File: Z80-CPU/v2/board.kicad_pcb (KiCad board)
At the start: 2 copper layers, 254 x 134.6 mm, 162 parts, among them K1 CONN_3, K2 CONN_3, K4 CONN_3, P1 S100_MALE, P2 CONN_4X2, P3 CLK_CPU, P34 CONN_1, P35 CONN_1, P36 CONN_3X2, P37 CONN_2X2, P4 CONN_2X2, P5 CLK_CPU, P6 CLK_SEL, Q1 2N3904, Q2 ^^NPN-SOT23, Q3 ^^NPN-SOT23, Q4 ^^NPN-SOT23, Q5 ^^NPN-SOT23, Q6 ^^NPN-SOT23, Q7 ^^NPN-SOT23, SW2 DIPS_08, SW3 DIPS_08, SW4 DIPS_08, U1 Z80, U10 74LS165, U11 74LS165, U12 74LS373, U13 2732, U14 74LS682N, U16 74LS273, U17 74LS273, U19 74LS244, U2 74LS373, U20 74LS244, U21 74LS244, U22 74LS373, U23 74LS02, U24 74LS04, U25 74LS04, U26 74LS05, U27 74LS139, U28 74LS00, U29 74LS74, U3 74LS373, U30 74LS74, U31 74LS00, U32 74LS74, U33 74LS74, U34 74LS74, U35 74LS32, U36 74LS04, U37 74LS05, U38 74F04, U39 74S08, U4 74LS153, U40 74S00, U41 74LS27, U42 2.0000 MHz, U43 74LS11, U44 74LS32, U45 74LS02, U47 74LS04, U48 LDO_REG_7805, U49 74LS00, U5 74LS157, U6 74LS153, U7 74LS32, U8 74LS157, U9 74LS165

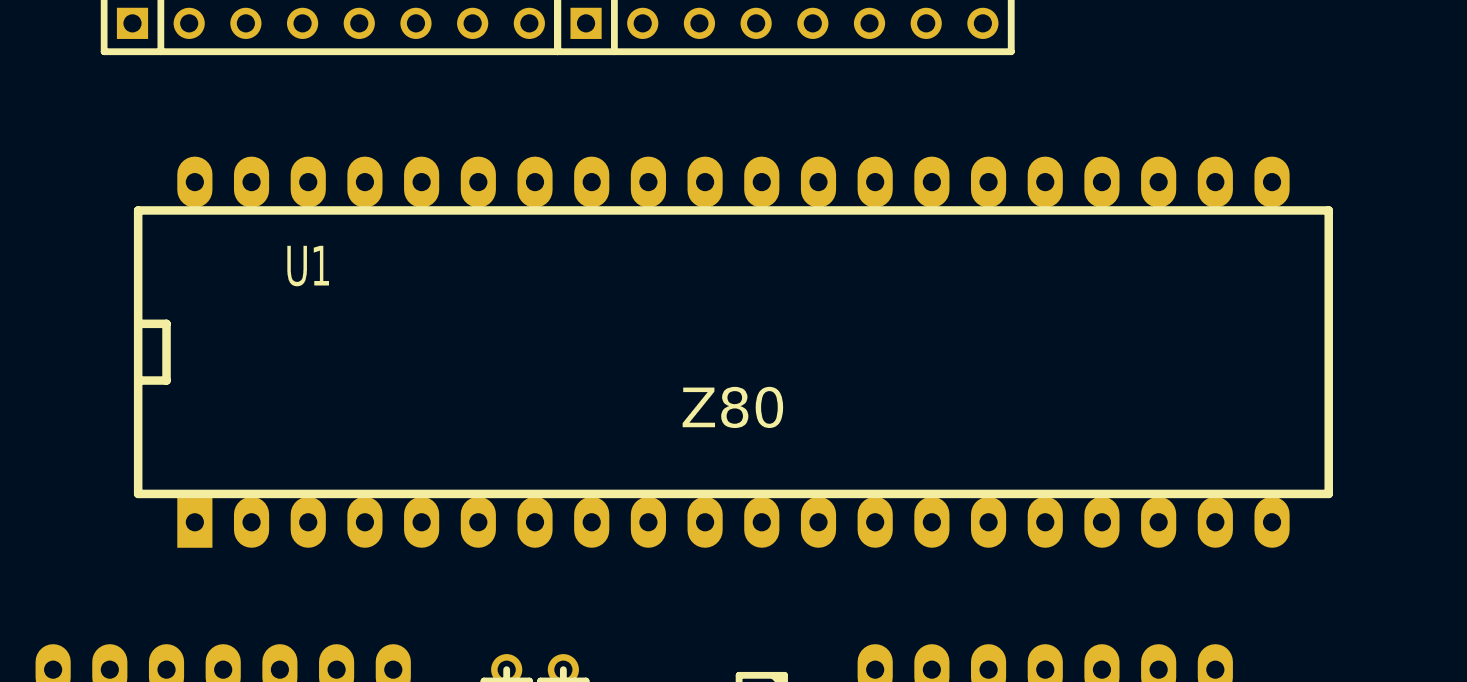
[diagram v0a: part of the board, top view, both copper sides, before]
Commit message: Z80-CPU v2: board layout (unrouted)
Source: S100 Z80 version2/backups/06-06-2014 2143
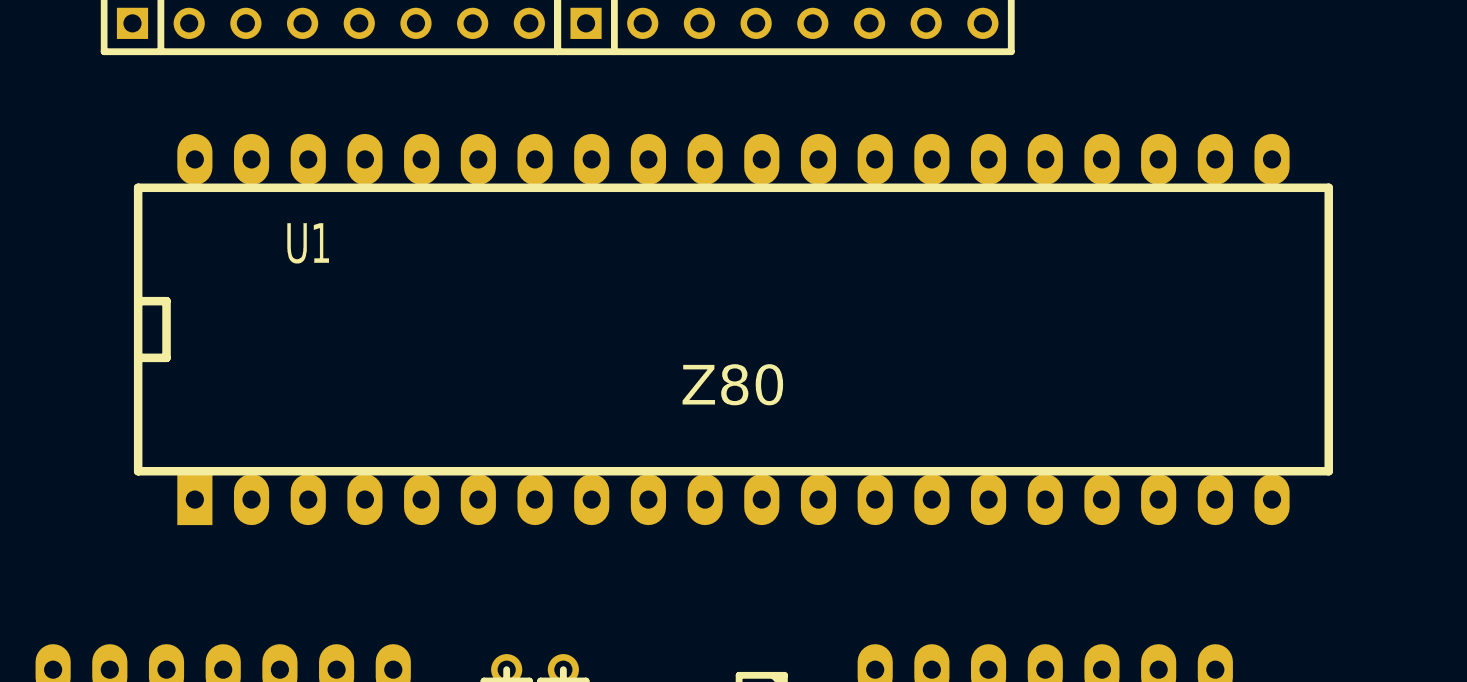
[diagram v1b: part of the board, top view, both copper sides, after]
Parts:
- moved U1 1.02 mm to (194.3, 55.9)
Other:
- net class Default: via_dia 0.5 -> 0.6
- net class gnd added: clearance 0.2032, trace_width 0.4, via_dia 0.6, via_drill 0.35
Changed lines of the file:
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@@
     (segment_width 0.381)
     (edge_width 0.381)
-    (via_size 0.5)
+    (via_size 0.6)
     (via_drill 0.35)
     (via_min_size 0.4)
@@
     (clearance 0.2032)
     (trace_width 0.2032)
-    (via_dia 0.5)
+    (via_dia 0.6)
     (via_drill 0.35)
     (uvia_dia 0.508)
@@
     (uvia_dia 0.508)
     (uvia_drill 0.2032)
-    (add_net GND)
     (add_net VCC)
   )
+  (net_class gnd ""
+    (clearance 0.2032)
+    (trace_width 0.4)
+    (via_dia 0.6)
+    (via_drill 0.35)
+    (uvia_dia 0.508)
+    (uvia_drill 0.2032)
+    (add_net GND)
+  )
   (net_class power8v ""
     (clearance 0.279)
@@
   )
   (module DIP-40__600_ELL (layer Component)
-    (at 194.31 56.896)
+    (at 194.31 55.88)
     (descr "Module Dil 40 pins, pads elliptiques, e=600 mils")
     (tags DIL)

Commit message: Z80-CPU v2: routed REV 1.0 board and gerbers
Source: S100 Z80 version2/GERBERS and S100 Z80 version2/board.kicad_pcb-bak.
The routed board at gerber time survives only as board.kicad_pcb-bak (saved 3 s before the gerbers); it is committed as board.kicad_pcb.
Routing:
- net GND: track 0.00 -> 2008.9 mm, vias 0 -> 27
- net VCC: track 0.00 -> 1321.4 mm
- net /D6: track 0.00 -> 427.9 mm, vias 0 -> 3
- net /D7: track 0.00 -> 424.7 mm, vias 0 -> 5
- net /PU1K-P: track 0.00 -> 413.5 mm, vias 0 -> 2
- net /IORQ: track 0.00 -> 399.4 mm, vias 0 -> 9
- net /START_SYNC: track 0.00 -> 389.6 mm, vias 0 -> 2
- net /D5: track 0.00 -> 353.5 mm, vias 0 -> 8
- net /pSYNC_RAW: track 0.00 -> 346.5 mm, vias 0 -> 3
- net /D1: track 0.00 -> 344.9 mm, vias 0 -> 7
- net /D4: track 0.00 -> 342.4 mm, vias 0 -> 6
- net /D0: track 0.00 -> 327.2 mm, vias 0 -> 4
- net /D3: track 0.00 -> 324.0 mm, vias 0 -> 8
- net /D2: track 0.00 -> 318.8 mm, vias 0 -> 6
- net N-00000177: track 0.00 -> 317.9 mm, vias 0 -> 2
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- added copper zone on B.Cu, net GND
- added copper zone on F.Cu, net GND
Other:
- board text added: "CLK 1"
- board text added: "CLK 2"
- board text added: "REV 1.0"
- board text added: "Z80 CPU BOARD"
- board text removed: "S-100 Z80 CPU BOARD VERSION 02"

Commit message: Z80-CPU v2: board edit (Z80cpuV3 logo trial, title text moved)
Source: S100 Z80 version2/board.kicad_pcb and board.pro (working folder, saved 2014-07-15).
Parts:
- added Z80cpuV3: , ***Z80cpuV3, F.Cu at (217.1, 142.3)
